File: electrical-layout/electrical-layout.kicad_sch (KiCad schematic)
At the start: 0 parts

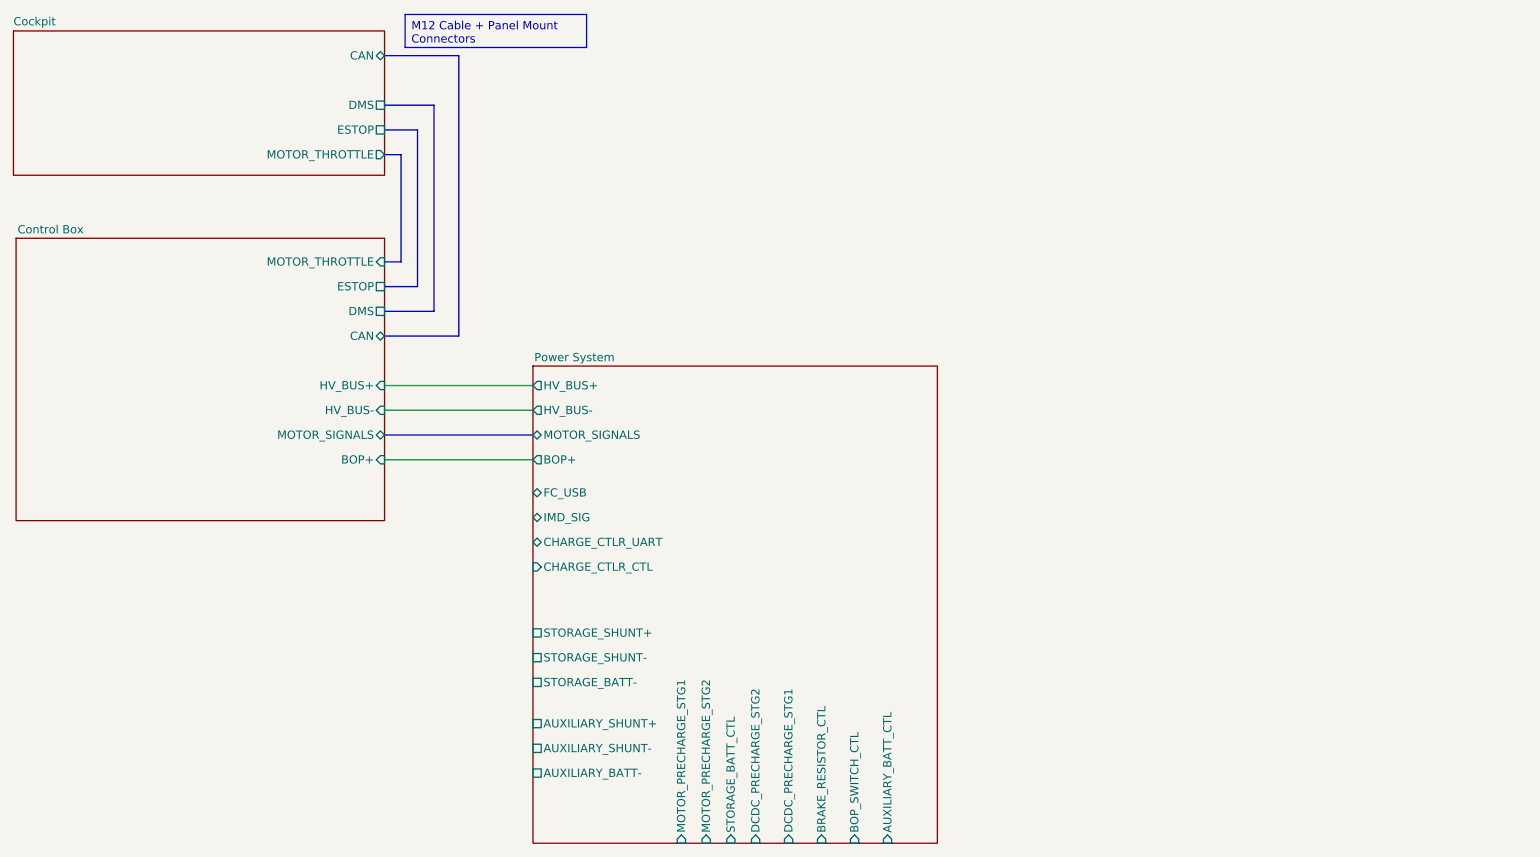
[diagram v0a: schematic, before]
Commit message: layout-2025: add power breadboard and connections
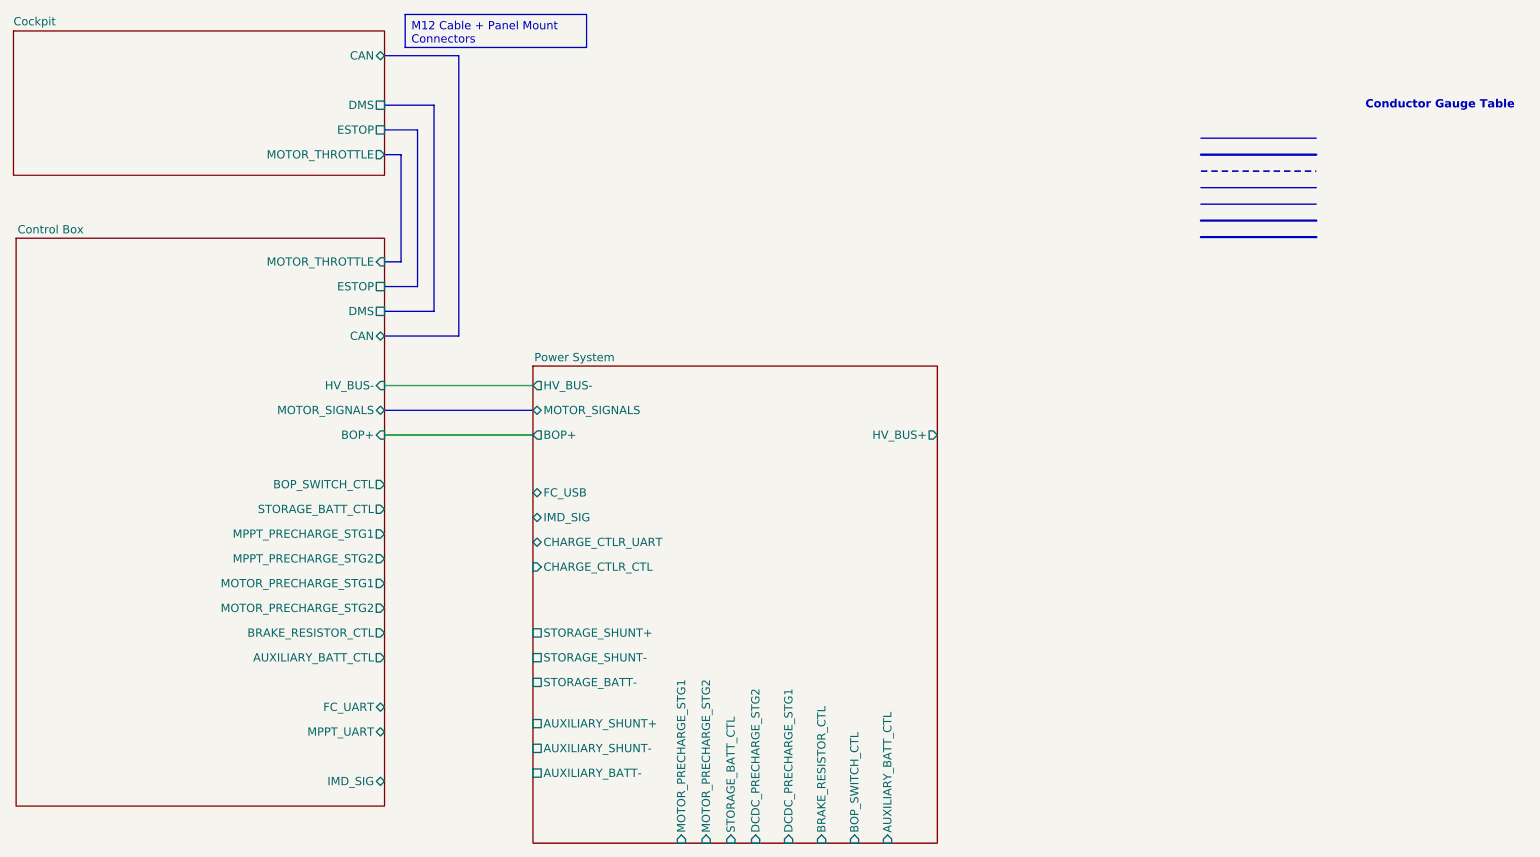
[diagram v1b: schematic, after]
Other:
- sheet Control Box ports: added AUXILIARY_BATT_CTL, BOP_SWITCH_CTL, BRAKE_RESISTOR_CTL, FC_UART, IMD_SIG, MOTOR_PRECHARGE_STG1, MOTOR_PRECHARGE_STG2, MPPT_PRECHARGE_STG1, MPPT_PRECHARGE_STG2, MPPT_UART, STORAGE_BATT_CTL; removed HV_BUS+
- note added: "Conductor Gauge Table"

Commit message: layout-2025: complete layout
- Added wire gauge from memory: must be checked once we get to the
  competition.
- Finalized all connections
- Moved a fuse
- Changed relay part number for some relays/contactors
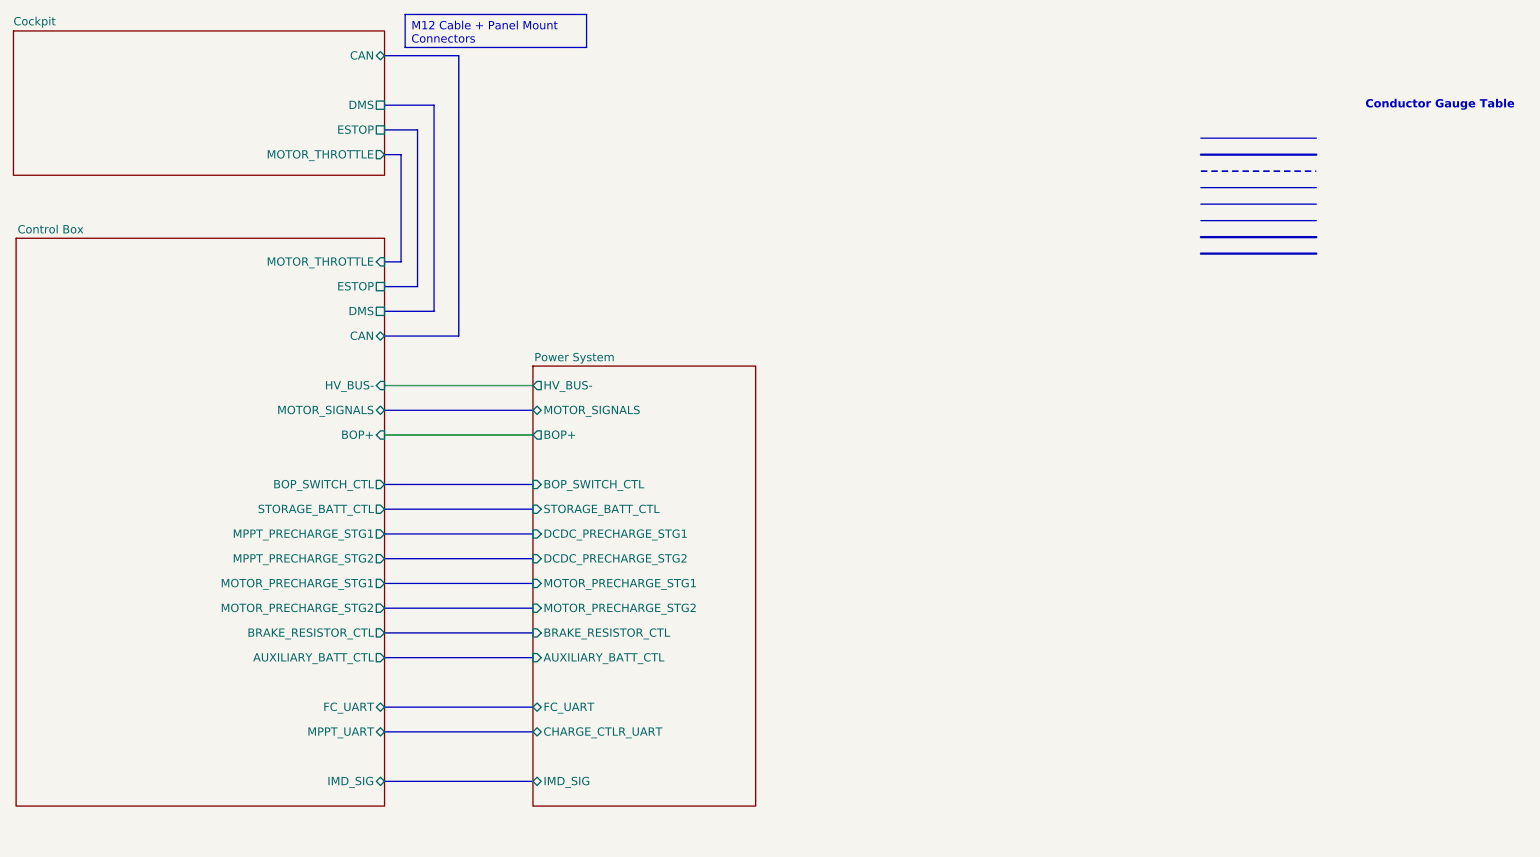
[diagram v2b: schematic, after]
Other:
- sheet Power System ports: added FC_UART; removed AUXILIARY_BATT-, AUXILIARY_SHUNT+, AUXILIARY_SHUNT-, CHARGE_CTLR_CTL, FC_USB, HV_BUS+, STORAGE_BATT-, STORAGE_SHUNT+, STORAGE_SHUNT-
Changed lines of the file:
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@@
+		)
+	)
+	(polyline
+		(pts
+			(xy 198.12 43.18) (xy 215.9 43.18)
+		)
+		(stroke
+			(width 0)
+			(type solid)
+			(color 194 194 0 1)
+		)
+	)
+	(bus
+		(pts
+			(xy 72.39 90.17) (xy 95.25 90.17)
+		)
+		(stroke
+			(width 0)
+			(type default)
 		)
 	)
@@
 		(pts
 			(xy 83.82 20.32) (xy 83.82 63.5)
+		)
+		(stroke
+			(width 0)
+			(type default)
+		)
+	)
+	(bus
+		(pts
+			(xy 72.39 124.46) (xy 95.25 124.46)
 		)
 		(stroke
@@
 	(bus
 		(pts
+			(xy 72.39 132.08) (xy 95.25 132.08)
+		)
+		(stroke
+			(width 0)
+			(type default)
+		)
+	)
+	(bus
+		(pts
+			(xy 72.39 101.6) (xy 95.25 101.6)
+		)
+		(stroke
+			(width 0)
+			(type default)
+		)
+	)
+	(bus
+		(pts
 			(xy 77.47 31.75) (xy 72.39 31.75)
 		)
@@
 	(polyline
 		(pts
-			(xy 198.12 45.72) (xy 215.9 45.72)
+			(xy 198.12 48.26) (xy 215.9 48.26)
 		)
 		(stroke
@@
 	(polyline
 		(pts
-			(xy 198.12 43.18) (xy 215.9 43.18)
+			(xy 198.12 45.72) (xy 215.9 45.72)
 		)
 		(stroke
@@
 	(bus
 		(pts
+			(xy 72.39 120.65) (xy 95.25 120.65)
+		)
+		(stroke
+			(width 0)
+			(type default)
+		)
+	)
+	(bus
+		(pts
+			(xy 72.39 93.98) (xy 95.25 93.98)
+		)
+		(stroke
+			(width 0)
+			(type default)
+		)
+	)
+	(bus
+		(pts
+			(xy 72.39 97.79) (xy 95.25 97.79)
+		)
+		(stroke
+			(width 0)
+			(type default)
+		)
+	)
+	(bus
+		(pts
 			(xy 74.93 35.56) (xy 74.93 52.07)
 		)
@@
 	(bus
 		(pts
+			(xy 72.39 105.41) (xy 95.25 105.41)
+		)
+		(stroke
+			(width 0)
+			(type default)
+		)
+	)
+	(bus
+		(pts
 			(xy 72.39 20.32) (xy 83.82 20.32)
 		)
@@
 	(bus
 		(pts
+			(xy 72.39 113.03) (xy 95.25 113.03)
+		)
+		(stroke
+			(width 0)
+			(type default)
+		)
+	)
+	(bus
+		(pts
 			(xy 80.01 59.69) (xy 80.01 27.94)
 		)
@@
 		)
 	)
+	(bus
+		(pts
+			(xy 72.39 109.22) (xy 95.25 109.22)
+		)
+		(stroke
+			(width 0)
+			(type default)
+		)
+	)
 	(wire
 		(pts
@@
 		)
 	)
+	(bus
+		(pts
+			(xy 72.39 86.36) (xy 95.25 86.36)
+		)
+		(stroke
+			(width 0)
+			(type default)
+		)
+	)
 	(polyline
 		(pts
-			(xy 198.12 48.26) (xy 215.9 48.26)
+			(xy 198.12 50.8) (xy 215.9 50.8)
 		)
 		(stroke
@@
 		)
 		(column_widths 22.86 58.42)
-		(row_heights 2.54 2.54 2.54 2.54 2.54 2.54 2.54 2.54)
+		(row_heights 2.54 2.54 2.54 2.54 2.54 2.54 2.54 2.54 2.54)
 		(cells
 			(table_cell "Color and format\n"
@@
 						(size 1.27 1.27)
 					)
-					(justify left top)
-				)
-			)
-			(table_cell "AWG #6 or larger"
+				)
+			)
+			(table_cell "2x AWG #12 or larger"
 				(exclude_from_sim no)
 				(at 218.44 41.91 0)
@@
 				)
 			)
-			(table_cell "2x AWG #6 or larger"
+			(table_cell "AWG #6 or larger"
 				(exclude_from_sim no)
 				(at 218.44 44.45 0)
@@
 				)
 			)
-			(table_cell "AWG #0 or larger"
+			(table_cell "2x AWG #6 or larger"
 				(exclude_from_sim no)
 				(at 218.44 46.99 0)
@@
 				)
 			)
+			(table_cell ""
+				(exclude_from_sim no)
+				(at 195.58 49.53 0)
+				(size 22.86 2.54)
+				(margins 0.9525 0.9525 0.9525 0.9525)
+				(span 1 1)
+				(fill
+					(type none)
+				)
+				(effects
+					(font
+						(size 1.27 1.27)
+					)
+					(justify left top)
+				)
+			)
+			(table_cell "AWG #0 or larger"
+				(exclude_from_sim no)
+				(at 218.44 49.53 0)
+				(size 58.42 2.54)
+				(margins 0.9525 0.9525 0.9525 0.9525)
+				(span 1 1)
+				(fill
+					(type none)
+				)
+				(effects
+					(font
+						(size 1.27 1.27)
+					)
+				)
+			)
 		)
 	)
 	(group ""
-		(members "00ff083b-dcf7-42a3-9cce-47a141e95711" "21356fc6-4374-41cf-8b75-c37691617742"
-			"37e29e43-a97e-445f-96c2-8c8af85a57cf" "461596d5-cf4b-4756-8cda-86153092ac6a"
-			"74052a3c-ce52-4a6c-9af1-5a6cf663aa58" "7dd42370-72e6-4492-bbea-1b1e22d8dcd8"
-			"828d14f1-af16-456c-9c34-7319c6f190a4" "93800c8c-424b-4fbb-b413-bebd9aedc25f"
-			"fe422dec-22dd-4f88-8af1-667bbbe32fd1"
+		(members "00ff083b-dcf7-42a3-9cce-47a141e95711" "02f3f634-44d6-4a0f-a999-1a7e26649312"
+			"21356fc6-4374-41cf-8b75-c37691617742" "37e29e43-a97e-445f-96c2-8c8af85a57cf"
+			"461596d5-cf4b-4756-8cda-86153092ac6a" "74052a3c-ce52-4a6c-9af1-5a6cf663aa58"
+			"7dd42370-72e6-4492-bbea-1b1e22d8dcd8" "828d14f1-af16-456c-9c34-7319c6f190a4"
+			"93800c8c-424b-4fbb-b413-bebd9aedc25f" "fe422dec-22dd-4f88-8af1-667bbbe32fd1"
 		)
 	)
@@
 	(sheet
 		(at 95.25 68.1209)
-		(size 62.2859 73.4841)
+		(size 34.2899 67.7691)
 		(exclude_from_sim no)
 		(in_bom yes)
@@
 			)
 		)
-		(pin "AUXILIARY_BATT-" passive
-			(at 95.25 130.81 180)
-			(effects
-				(font
-					(size 1.27 1.27)
-				)
-				(justify left)
-			)
-		)
 		(pin "AUXILIARY_BATT_CTL" input
-			(at 149.86 141.605 270)
-			(effects
-				(font
-					(size 1.27 1.27)
-				)
-				(justify left)
-			)
-		)
-		(pin "AUXILIARY_SHUNT+" passive
-			(at 95.25 123.19 180)
-			(effects
-				(font
-					(size 1.27 1.27)
-				)
-				(justify left)
-			)
-		)
-		(pin "AUXILIARY_SHUNT-" passive
-			(at 95.25 127 180)
+			(at 95.25 113.03 180)
 			(effects
 				(font
@@
 		)
 		(pin "BOP_SWITCH_CTL" input
-			(at 144.78 141.605 270)
+			(at 95.25 86.36 180)
 			(effects
 				(font
@@
 		)
 		(pin "BRAKE_RESISTOR_CTL" input
-			(at 139.7 141.605 270)
-			(effects
-				(font
-					(size 1.27 1.27)
-				)
-				(justify left)
-			)
-		)
-		(pin "CHARGE_CTLR_CTL" input
-			(at 95.25 99.06 180)
+			(at 95.25 109.22 180)
 			(effects
 				(font
@@
 		)
 		(pin "CHARGE_CTLR_UART" bidirectional
-			(at 95.25 95.25 180)
+			(at 95.25 124.46 180)
 			(effects
 				(font
@@
 		)
 		(pin "DCDC_PRECHARGE_STG1" input
-			(at 134.62 141.605 270)
+			(at 95.25 93.98 180)
 			(effects
 				(font
@@
 		)
 		(pin "DCDC_PRECHARGE_STG2" input
-			(at 129.54 141.605 270)
-			(effects
-				(font
-					(size 1.27 1.27)
-				)
-				(justify left)
-			)
-		)
-		(pin "FC_USB" bidirectional
-			(at 95.25 87.63 180)
-			(effects
-				(font
-					(size 1.27 1.27)
-				)
-				(justify left)
-			)
-		)
-		(pin "HV_BUS+" output
-			(at 157.5359 78.74 0)
-			(effects
-				(font
-					(size 1.27 1.27)
-				)
-				(justify right)
+			(at 95.25 97.79 180)
+			(effects
+				(font
+					(size 1.27 1.27)
+				)
+				(justify left)
 			)
 		)
@@
 		)
 		(pin "IMD_SIG" bidirectional
-			(at 95.25 91.44 180)
+			(at 95.25 132.08 180)
 			(effects
 				(font
@@
 		)
 		(pin "MOTOR_PRECHARGE_STG1" input
-			(at 118.11 141.605 270)
+			(at 95.25 101.6 180)
 			(effects
 				(font
@@
 		)
 		(pin "MOTOR_PRECHARGE_STG2" input
-			(at 121.92 141.605 270)
+			(at 95.25 105.41 180)
 			(effects
 				(font
@@
 			)
 		)
-		(pin "STORAGE_BATT-" passive
-			(at 95.25 116.84 180)
-			(effects
-				(font
-					(size 1.27 1.27)
-				)
-				(justify left)
-			)
-		)
 		(pin "STORAGE_BATT_CTL" input
-			(at 125.73 141.605 270)
-			(effects
-				(font
-					(size 1.27 1.27)
-				)
-				(justify left)
-			)
-		)
-		(pin "STORAGE_SHUNT+" passive
-			(at 95.25 109.22 180)
-			(effects
-				(font
-					(size 1.27 1.27)
-				)
-				(justify left)
-			)
-		)
-		(pin "STORAGE_SHUNT-" passive
-			(at 95.25 113.03 180)
+			(at 95.25 90.17 180)
 			(effects
 				(font
@@
 			(effects
 				(font
+					(size 1.27 1.27)
+				)
+				(justify left)
+			)
+		)
+		(pin "FC_UART" bidirectional
+			(at 95.25 120.65 180)
+			(effects
+				(font
